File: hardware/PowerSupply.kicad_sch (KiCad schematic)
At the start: 0 parts

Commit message: Populate Power Supply sheet
Full input-protection-through-3.3V chain, wired and datasheet-verified:
- Input protection: screw terminals, TVS (SMBJ48CA-13-F), high-side
  N-ch ORing/reverse-polarity block (LM5050-1 + NTMFS006N08MC)
- Input eFuse: TI TPS1689x (PTPS16890VMAR), wired per the real TI
  datasheet (fetched SLVSHO1A directly) in standalone/non-PMBus config
  - EN/UVLO divider computed for ~10V trip, ILIM/IMON set OCP ~18.3A
  - Found and worked around a real vendor symbol defect: pin 20 is
    defined twice (SWEN + WP#) at two different physical locations
- Buck: LMR38020 (12-36V -> 5V, 2A), wired per the real TI datasheet
  (SNVSC40E) at ~1.1MHz switching, FB divider computed for 5.01V
- LDO: NCP1117-3.3 (5V -> 3.3V), standard app circuit
- 4x PWR_FLAG markers added where ERC's power-driver check doesn't
  understand pass-through/sense-only topologies
- ARCHITECTURE.md updated with final as-built values (several
  substituted to nearest available library value where the exact
  datasheet-recommended value doesn't exist in ChipResistors/
  Capacitors) and known residual ERC items

Co-Authored-By: Claude Sonnet 5 <noreply@anthropic.com>
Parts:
- added C10, C11, C17: 100 nF, symbol METUPowerLab_Capacitors_Ceramics_SurfaceMounts:100 nF
- added C12, C14: 1 nF, symbol METUPowerLab_Capacitors_Ceramics_SurfaceMounts:1 nF
- added C13: 10 nF, symbol METUPowerLab_Capacitors_Ceramics_SurfaceMounts:10 nF
- added C15: 22 pF, symbol METUPowerLab_Capacitors_Ceramics_SurfaceMounts:22 pF
- added C16: 4.7 µF, symbol METUPowerLab_Capacitors_Ceramics_SurfaceMounts:4.7 µF
- added C18: BOOT 100nF 16V+, symbol METUPowerLab_Capacitors_Ceramics_SurfaceMounts:100 nF
- added C19, C20: 22 µF, symbol METUPowerLab_Capacitors_Ceramics_SurfaceMounts:22 µF
- added C21: 1 µF, symbol METUPowerLab_Capacitors_Ceramics_SurfaceMounts:1 µF
- added C22: 10 µF, symbol METUPowerLab_Capacitors_Ceramics_SurfaceMounts:10 µF
- added D1: SMBJ48CA-13-F, METUPowerLab_Diodes_TVSDiodes:DO-214AA, symbol METUPowerLab_Diodes_TVSDiodes:SMBJ48CA-13-F
- added J3: VIN+, METUPowerLab_Connectors_ScrewTerminals:7770, symbol METUPowerLab_Connectors_ScrewTerminals:7770
- added J4: GND, METUPowerLab_Connectors_ScrewTerminals:7770, symbol METUPowerLab_Connectors_ScrewTerminals:7770
- added L1: 6.8µH, symbol METUPowerLab_Inductors_SurfaceMounts:6.8µH
- added Q1: RevPol, METUPowerLab_Transistors_MOSFETs:8-PowerTDFN(5x6mm), symbol METUPowerLab_Transistors_MOSFETs:NTMFS006N08MC
- added R10, R11, R9: 10 kOhm, symbol METUPowerLab_Resistors_ChipResistors:10 kOhm
- added R12: RT 22.1k (~1.1MHz), symbol METUPowerLab_Resistors_ChipResistors:22.1 kOhm
- added R13: 88.7 kOhm, symbol METUPowerLab_Resistors_ChipResistors:88.7 kOhm
- added R14: 22.1 kOhm, symbol METUPowerLab_Resistors_ChipResistors:22.1 kOhm
- added R15: 100 kOhm, symbol METUPowerLab_Resistors_ChipResistors:100 kOhm
- added R4: 120 Ohm, symbol METUPowerLab_Resistors_ChipResistors:120 Ohm
- added R5: 866 kOhm, symbol METUPowerLab_Resistors_ChipResistors:866 kOhm
- added R6: 118 kOhm, symbol METUPowerLab_Resistors_ChipResistors:118 kOhm
- added R7: 1.2 kOhm, symbol METUPowerLab_Resistors_ChipResistors:1.2 kOhm
- added R8: 3 kOhm, symbol METUPowerLab_Resistors_ChipResistors:3 kOhm
- added U2: LM5050-1, METUPowerLab_CircuitProtections_IdealDiodes:SOT-23-6, symbol METUPowerLab_CircuitProtections_IdealDiodes:LM5050-1
- added U3: PTPS16890VMAR, METUPowerLab_CircuitProtections_eFuses:23-LQFN-CLIP_(VMA), symbol METUPowerLab_CircuitProtections_eFuses:PTPS16890VMAR
- added U4: LMR38020FSDDAR, METUPowerLab_Regulators_BuckConverters:8-SOICPower, symbol METUPowerLab_Regulators_BuckConverters:LMR38020FSDDAR
- added U5: NCP1117ST33T3G, METUPowerLab_Regulators_LDOs:SOT-223, symbol METUPowerLab_Regulators_LDOs:NCP1117ST33T3G
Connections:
- new net +3V3_MCU: C22.1, R10.2, R11.2, U5.2 (OUTPUT)
- new net +5V_LOGIC: C16.1, C17.1, C19.1, C20.1, C21.1, L1.2, R13.1, R15.1, U3.7 (OUT), U3.8 (OUT), U4.2 (EN), U4.3 (VIN), U5.3 (INPUT)
- new net +VBUS: Q1.1 (S), R4.1, R5.1, U2.1 (VS), U2.6 (OUT), U3.10 (IN), U3.22 (IN), U3.23 (IN), U3.24 (IN)
- new net BUCK_BOOT: C18.1, U4.7 (BOOT)
- new net BUCK_FB: R13.2, R14.1, U4.5 (FB)
- new net BUCK_PG: R15.2, U4.6 (PG)
- new net BUCK_RT: R12.1, U4.4 (RT/SYNC)
- new net BUCK_SW: C18.2, L1.1, U4.8 (SW)
- new net EFUSE_AUX: R9.1, U3.14 (AUX/EEDATA/_GPIO2)
- new net EFUSE_DVDT: C13.1, U3.4 (dV/dT)
- new net EFUSE_ENUVLO: C11.1, R5.2, R6.1, U3.16 (EN/UVLO)
- new net EFUSE_ILIM: R7.1, U3.1 (ILIM)
- new net EFUSE_IREF: C12.1, U3.3 (IREF)
- new net EFUSE_SCL: R11.1, U3.12 (SCL)
- new net EFUSE_SDA: R10.1, U3.11 (SDA)
- new net EFUSE_TEMP: C14.1, U3.15 (TEMP/EECLK/_GPIO1)
- new net EFUSE_VDD: C10.1, R4.2, U3.9 (VDD)
- new net GND: C10.2, C11.2, C12.2, C13.2, C14.2, C15.1, C15.2, C16.2, C17.2, C19.2, C20.2, C21.2, C22.2, D1.2, J4.1, R12.2, R14.2, R6.2, R7.2, R8.1, R8.2, R9.2, U2.2 (GND), U2.3 (OFF), U3.18 (ADDR1), U3.2 (IMON), U3.20 (WP#), U3.5 (GND), U3.6 (ADDR0), U4.1 (GND), U4.Shield, U5.1 (GND)
- new net REVPOL_GATE: Q1.2 (G), U2.5 (GATE)
- new net VIN_RAW: D1.1, J3.1, Q1.3 (D), U2.4 (IN)
- no-connect marks 0 -> 2

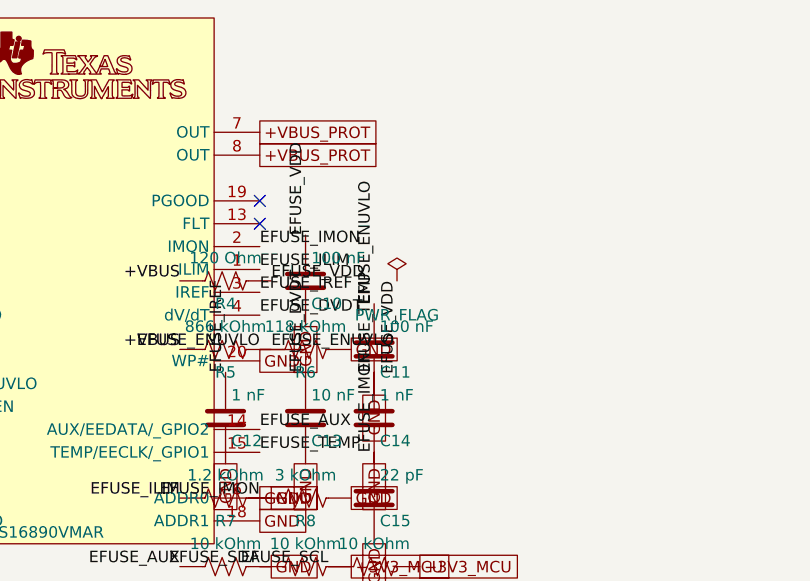
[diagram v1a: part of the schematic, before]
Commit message: Populate Current Sensing + Communication sheets; schematic complete
Current Sensing:
- DC-bus shunt (5 mOhm, in series after the eFuse - required renaming
  the eFuse OUT net to +VBUS_EFUSE_OUT so the shunt sits properly
  in-line ahead of +VBUS_PROT)
- INA240 total-bus current sense, unidirectional config, -> MCU ADC

Communication:
- SN65HVD230 CAN transceiver (3.3V native) on ESP32 TWAI pins
- Per-line TVS (SP0115-01UTG) on CANH/CANL
- 4-pin bus connector (CANH/CANL/GND/+VBUS_PROT)

Whole-hierarchy ERC (all 6 sheets + root) now down to 3 residual
errors, all the same benign/expected 'two power_out pins on one net'
pattern (datasheet-recommended parallel pins, or a PWR_FLAG sharing
a net with a real driver) - fully explained in ARCHITECTURE.md, which
now also documents the found-and-worked-around vendor library defects
(eFuse pin-20 duplication, TMP235 VOUT mistyped as input) and confirms
the shunt 'duplicate pins' are correct 4-terminal Kelvin modeling, not
a bug.

All 6 hierarchical sheets are now fully wired end to end:
Power Supply -> MCU Core -> Gate Drive -> Power Stage, with Current
Sensing and Communication cross-wired throughout.

Co-Authored-By: Claude Sonnet 5 <noreply@anthropic.com>
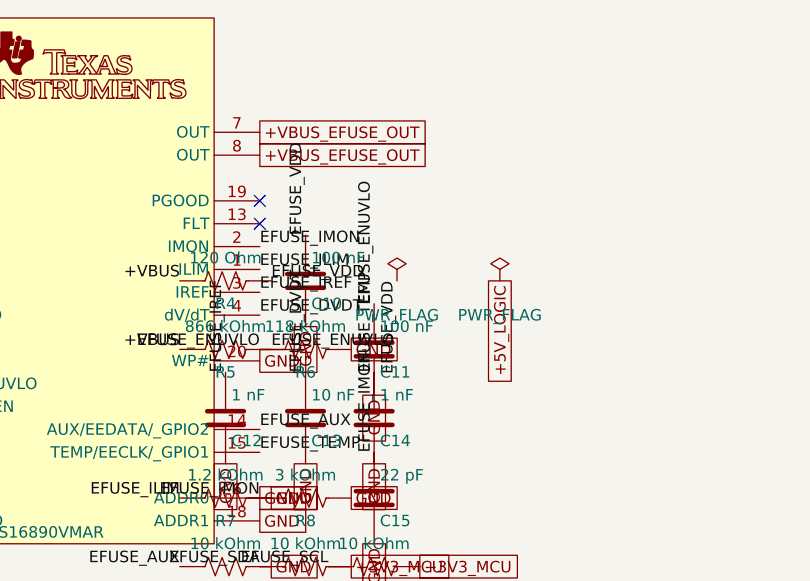
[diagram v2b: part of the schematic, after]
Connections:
- net +5V_LOGIC: no longer U3.7 (OUT), U3.8 (OUT)
- new net +VBUS_EFUSE_OUT: U3.7 (OUT), U3.8 (OUT)
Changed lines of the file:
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@@
-		)
-	)
-	(global_label "+VBUS_PROT"
-		(at 133.35 13.969999999999999 0)
-		(effects
-			(font
-				(size 1.27 1.27)
-			)
-			(justify left)
-		)
-	)
-	(global_label "+VBUS_PROT"
-		(at 133.35 16.509999999999998 0)
-		(effects
-			(font
-				(size 1.27 1.27)
-			)
-			(justify left)
 		)
 	)
@@
 		(effects
 			(font
+				(size 1.27 1.27)
+			)
+			(justify right)
+		)
+	)
+	(global_label "+VBUS_EFUSE_OUT"
+		(at 133.35 13.969999999999999 0)
+		(effects
+			(font
+				(size 1.27 1.27)
+			)
+			(justify left)
+		)
+	)
+	(global_label "+VBUS_EFUSE_OUT"
+		(at 133.35 16.509999999999998 0)
+		(effects
+			(font
+				(size 1.27 1.27)
+			)
+			(justify left)
+		)
+	)
+	(symbol
+		(lib_id "power:PWR_FLAG")
+		(at 160.02 30.48 0)
+		(unit 1)
+		(body_style 1)
+		(exclude_from_sim no)
+		(in_bom yes)
+		(on_board yes)
+		(in_pos_files yes)
+		(dnp no)
+		(property "Reference" "#FLG5"
+			(at 160.02 32.385 0)
+			(hide yes)
+			(show_name no)
+			(do_not_autoplace no)
+			(effects
+				(font
+					(size 1.27 1.27)
+				)
+			)
+		)
+		(property "Value" "PWR_FLAG"
+			(at 160.02 34.29 0)
+			(show_name no)
+			(do_not_autoplace no)
+			(effects
+				(font
+					(size 1.27 1.27)
+				)
+			)
+		)
+		(property "Footprint" ""
+			(at 160.02 30.48 0)
+			(hide yes)
+			(show_name no)
+			(do_not_autoplace no)
+			(effects
+				(font
+					(size 1.27 1.27)
+				)
+			)
+		)
+		(property "Datasheet" ""
+			(at 160.02 30.48 0)
+			(hide yes)
+			(show_name no)
+			(do_not_autoplace no)
+			(effects
+				(font
+					(size 1.27 1.27)
+				)
+			)
+		)
+		(property "Description" "Special symbol for telling ERC where power comes from"
+			(at 160.02 30.48 0)
+			(hide yes)
+			(show_name no)
+			(do_not_autoplace no)
+			(effects
+				(font
+					(size 1.27 1.27)
+				)
+			)
+		)
+		(pin "1"
+		)
+		(instances
+			(project "ESC3Phase"
+				(path "/346bb8fa-d8d5-4112-bc90-d433fe541041"
+					(reference "#FLG5")
+					(unit 1)
+				)
+			)
+		)
+	)
+	(global_label "+5V_LOGIC"
+		(at 160.02 30.48 270)
+		(effects
+			(font

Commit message: PCB layout: board outline, mounting holes, footprint placement, copper pours, phase-output routing
- 100x115mm 2-layer board, 4x M3 mounting holes, design rules per PowerLab spec
- All 55 schematic components synced to board with real footprints
- Auto-placed via force-directed placement with locked connector/MCU anchors
- GND pour (both layers) + localized pours for VIN_RAW/+VBUS/+VBUS_EFUSE_OUT/+VBUS_PROT/+5V_LOGIC
- Routed the 3 critical phase-output traces (SHA/SHB/SHC, 2mm wide)
- Documented full PCB status in ARCHITECTURE.md: NOT yet fab-ready (732 DRC
  violations, 21 courtyard overlaps, ~50 signal nets still unrouted since
  Freerouting is unavailable in this environment)

Co-Authored-By: Claude Sonnet 5 <noreply@anthropic.com>
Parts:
- C10, C11, C12, C13, C14, C15, C17, C18, C21: footprint (none) -> METUPowerLab_Capacitors_Ceramics_SurfaceMounts:0603_Medium
- C16, C22: footprint (none) -> METUPowerLab_Capacitors_Ceramics_SurfaceMounts:0805_Medium
- C19, C20: footprint (none) -> METUPowerLab_Capacitors_Ceramics_SurfaceMounts:1210_Medium
- L1: footprint (none) -> METUPowerLab_Inductors_SurfaceMounts:6x6mm
- R10, R11, R12, R13, R14, R15, R4, R5, R6, R7, R8, R9: footprint (none) -> METUPowerLab_Resistors_ChipResistors:0603_Medium
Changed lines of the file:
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@@
 			)
 		)
-		(property "Footprint" ""
+		(property "Footprint" "METUPowerLab_Capacitors_Ceramics_SurfaceMounts:0603_Medium"
 			(at 147.015 34.29 0)
 			(hide yes)
@@
 			)
 		)
-		(property "Footprint" ""
+		(property "Footprint" "METUPowerLab_Capacitors_Ceramics_SurfaceMounts:0603_Medium"
 			(at 139.395 41.91 0)
 			(hide yes)
@@
 			)
 		)
-		(property "Footprint" ""
+		(property "Footprint" "METUPowerLab_Capacitors_Ceramics_SurfaceMounts:0603_Medium"
 			(at 147.015 50.8 0)
 			(hide yes)
@@
 			)
 		)
-		(property "Footprint" ""
+		(property "Footprint" "METUPowerLab_Resistors_ChipResistors:0603_Medium"
 			(at 130.556 61.976 90)
 			(hide yes)
@@
 			)
 		)
-		(property "Footprint" ""
+		(property "Footprint" "METUPowerLab_Resistors_ChipResistors:0603_Medium"
 			(at 139.446 61.976 90)
 			(hide yes)
@@
 			)
 		)
-		(property "Footprint" ""
+		(property "Footprint" "METUPowerLab_Resistors_ChipResistors:0603_Medium"
 			(at 147.066 61.976 90)
 			(hide yes)
@@
 			)
 		)
-		(property "Footprint" ""
+		(property "Footprint" "METUPowerLab_Resistors_ChipResistors:0603_Medium"
 			(at 130.556 30.226 90)
 			(hide yes)
@@
 			)
 		)
-		(property "Footprint" ""
+		(property "Footprint" "METUPowerLab_Capacitors_Ceramics_SurfaceMounts:0603_Medium"
 			(at 139.395 26.67 0)
 			(hide yes)
@@
 			)
 		)
-		(property "Footprint" ""
+		(property "Footprint" "METUPowerLab_Resistors_ChipResistors:0603_Medium"
 			(at 130.556 37.846 90)
 			(hide yes)
@@
 			)
 		)
-		(property "Footprint" ""
+		(property "Footprint" "METUPowerLab_Resistors_ChipResistors:0603_Medium"
 			(at 139.446 37.846 90)
 			(hide yes)
@@
 			)
 		)
-		(property "Footprint" ""
+		(property "Footprint" "METUPowerLab_Resistors_ChipResistors:0603_Medium"
 			(at 130.556 54.356 90)
 			(hide yes)
@@
 			)
 		)
-		(property "Footprint" ""
+		(property "Footprint" "METUPowerLab_Resistors_ChipResistors:0603_Medium"
 			(at 139.446 54.356 90)
 			(hide yes)
@@
 			)
 		)
-		(property "Footprint" ""
+		(property "Footprint" "METUPowerLab_Capacitors_Ceramics_SurfaceMounts:0603_Medium"
 			(at 130.505 41.91 0)
 			(hide yes)
@@
 			)
 		)
-		(property "Footprint" ""
+		(property "Footprint" "METUPowerLab_Capacitors_Ceramics_SurfaceMounts:0603_Medium"
 			(at 147.015 41.91 0)
 			(hide yes)
@@
 			)
 		)
-		(property "Footprint" ""
+		(property "Footprint" "METUPowerLab_Capacitors_Ceramics_SurfaceMounts:0805_Medium"
 			(at 80.975 86.36 0)
 			(hide yes)
@@
 			)
 		)
-		(property "Footprint" ""
+		(property "Footprint" "METUPowerLab_Capacitors_Ceramics_SurfaceMounts:0603_Medium"
 			(at 88.595 86.36 0)
 			(hide yes)
@@
 			)
 		)
-		(property "Footprint" ""
+		(property "Footprint" "METUPowerLab_Resistors_ChipResistors:0603_Medium"
 			(at 88.646 111.506 90)
 			(hide yes)
@@
 			)
 		)
-		(property "Footprint" ""
+		(property "Footprint" "METUPowerLab_Resistors_ChipResistors:0603_Medium"
 			(at 130.556 96.266 90)
 			(hide yes)
@@
 			)
 		)
-		(property "Footprint" ""
+		(property "Footprint" "METUPowerLab_Resistors_ChipResistors:0603_Medium"
 			(at 130.556 103.886 90)
 			(hide yes)
@@
 			)
 		)
-		(property "Footprint" ""
+		(property "Footprint" "METUPowerLab_Resistors_ChipResistors:0603_Medium"
 			(at 101.346 87.376 90)
 			(hide yes)
@@
 			)
 		)
-		(property "Footprint" ""
+		(property "Footprint" "METUPowerLab_Capacitors_Ceramics_SurfaceMounts:0603_Medium"
 			(at 112.725 87.63 0)
 			(hide yes)
@@
 			)
 		)
-		(property "Footprint" ""
+		(property "Footprint" "METUPowerLab_Inductors_SurfaceMounts:6x6mm"
 			(at 121.92 100.33 0)
 			(hide yes)
@@
 			)
 		)
-		(property "Footprint" ""
+		(property "Footprint" "METUPowerLab_Capacitors_Ceramics_SurfaceMounts:1210_Medium"
 			(at 139.395 96.52 0)
 			(hide yes)
@@
 			)
 		)
-		(property "Footprint" ""
+		(property "Footprint" "METUPowerLab_Capacitors_Ceramics_SurfaceMounts:1210_Medium"
 			(at 147.015 96.52 0)
 			(hide yes)
@@
 			)
 		)
-		(property "Footprint" ""
+		(property "Footprint" "METUPowerLab_Capacitors_Ceramics_SurfaceMounts:0603_Medium"
 			(at 155.905 86.36 0)
 			(hide yes)
@@
 			)
 		)
-		(property "Footprint" ""
+		(property "Footprint" "METUPowerLab_Capacitors_Ceramics_SurfaceMounts:0805_Medium"
 			(at 172.415 86.36 0)
 			(hide yes)
